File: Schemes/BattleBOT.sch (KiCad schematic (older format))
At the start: 16 parts

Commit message: make changes to Schemes
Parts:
- removed 1kΩ, 2.2kΩ: R, symbol Device:R
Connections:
- net +12V: no longer U?.~ (Vin)
- net at U?.1 (MotorB): now also M?.1 (+)
- net at U?.2: now also M?.2 (-)
- new net: U?.~ (IN3), U?.~ (Vin) (x9)
- new net: U?.~ (VCC), U?.~ (Vin)
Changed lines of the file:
@@
 Wire Wire Line
 	2650 1600 2650 1800
-Wire Wire Line
-	2650 2400 3000 2400
 $Comp
 L pspice:0 #GND?
@@
 Connection ~ 2650 1800
 Wire Wire Line
-	2650 1800 2650 2400
-Wire Wire Line
 	2650 1800 4250 1800
 Wire Wire Line
@@
 	3250 5150 3250 5100
 Wire Wire Line
-	4000 2750 6300 2750
-Wire Wire Line
-	6300 2750 6300 1750
-Wire Wire Line
-	6200 1750 6200 2600
-Wire Wire Line
-	6200 2600 4000 2600
-Wire Wire Line
 	4000 3000 6600 3000
 Wire Wire Line
 	6600 3000 6600 1750
-Wire Wire Line
-	6400 1750 6400 3200
-Wire Wire Line
-	6400 3200 4000 3200
-Wire Wire Line
-	6500 1750 6500 3300
-Wire Wire Line
-	6500 3300 4000 3300
 Wire Wire Line
 	4550 5900 6000 5900
@@
 Wire Wire Line
 	10550 1450 10550 2000
-Wire Wire Line
-	9550 2000 9100 2000
 $Comp
 L Device:R 1kΩ
@@
 	1    0    0    -1
 $EndComp
-$Comp
-L Device:R 1kΩ
-U 1 1 5E9473A1
-P 7850 2850
-F 0 "1kΩ" H 7920 2896 50  0000 L CNN
-F 1 "R" H 7920 2805 50  0000 L CNN
-F 2 "" V 7780 2850 50  0001 C CNN
-F 3 "~" H 7850 2850 50  0001 C CNN
-	1    7850 2850
-	1    0    0    -1
-$EndComp
-$Comp
-L Device:R 2.2kΩ
-U 1 1 5E9479C3
-P 7850 3150
-F 0 "2.2kΩ" H 7920 3196 50  0000 L CNN
-F 1 "R" H 7920 3105 50  0000 L CNN
-F 2 "" V 7780 3150 50  0001 C CNN
-F 3 "~" H 7850 3150 50  0001 C CNN
-	1    7850 3150
-	1    0    0    -1
-$EndComp
 Wire Wire Line
 	6100 1750 6100 3100
 Wire Wire Line
 	6100 3100 4000 3100
-Wire Wire Line
-	7850 1950 7850 1800
 Wire Wire Line
 	7850 650  4250 650
@@
 	4250 1800 5800 1800
 Wire Wire Line
-	7850 1800 7500 1800
-Wire Wire Line
-	7500 1800 7500 2700
-Wire Wire Line
-	7500 2700 7850 2700
-Connection ~ 7850 1800
-Wire Wire Line
-	7850 1800 7850 650
-Wire Wire Line
-	7850 2550 8550 2550
-Wire Wire Line
-	8550 2550 8550 3400
-Wire Wire Line
-	8550 3400 7850 3400
-Wire Wire Line
-	7850 3400 7850 3300
-$Comp
-L pspice:0 #GND?
-U 1 1 5EC7A03C
-P 7850 3600
-F 0 "#GND?" H 7850 3500 50  0001 C CNN
-F 1 "0" H 7850 3689 50  0000 C CNN
-F 2 "" H 7850 3600 50  0001 C CNN
-F 3 "~" H 7850 3600 50  0001 C CNN
-	1    7850 3600
-	1    0    0    -1
-$EndComp
-Wire Wire Line
-	7850 3400 7850 3600
-Connection ~ 7850 3400
-Wire Wire Line
-	4000 4000 7500 4000
-Wire Wire Line
-	7500 4000 7500 3000
-Wire Wire Line
-	7500 3000 7850 3000
-Connection ~ 7850 3000
-Wire Wire Line
 	4000 3900 7300 3900
 Wire Wire Line
@@
 Connection ~ 7850 2250
 Wire Wire Line
-	7850 2250 9100 2250
-Wire Wire Line
-	9100 2250 9100 2000
-Wire Wire Line
-	8950 3000 8950 1450
-Wire Wire Line
-	7850 3000 8950 3000
-Wire Wire Line
 	8950 1450 10550 1450
+Wire Wire Line
+	6000 1750 6000 2100
+Wire Wire Line
+	6000 2100 3000 2100
+Wire Wire Line
+	3000 2100 3000 2400
+Wire Wire Line
+	7850 650  7850 1950
+$Comp
+L pspice:0 #GND?
+U 1 1 5EC82388
+P 7850 2700
+F 0 "#GND?" H 7850 2600 50  0001 C CNN
+F 1 "0" H 7850 2789 50  0000 C CNN
+F 2 "" H 7850 2700 50  0001 C CNN
+F 3 "~" H 7850 2700 50  0001 C CNN
+	1    7850 2700
+	1    0    0    -1
+$EndComp
+Wire Wire Line
+	7850 2550 7850 2700
+Wire Wire Line
+	4000 4000 7500 4000
+Wire Wire Line
+	7500 4000 7500 2800
+Wire Wire Line
+	7500 2800 8950 2800
+Wire Wire Line
+	8950 2800 8950 1450
+Wire Wire Line
+	8650 2250 8650 2000
+Wire Wire Line
+	8650 2000 9550 2000
+Wire Wire Line
+	7850 2250 8650 2250
+Wire Wire Line
+	4000 3200 6200 3200
+Wire Wire Line
+	6200 3200 6200 1750
+Wire Wire Line
+	4000 3300 6300 3300
+Wire Wire Line
+	6300 3300 6300 1750
+Wire Wire Line
+	4000 3400 6500 3400
+Wire Wire Line
+	6500 3400 6500 1750
+Wire Wire Line
+	4000 3500 6400 3500
+Wire Wire Line
+	6400 3500 6400 1750
 $EndSCHEMATC

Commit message: make changes to schemes
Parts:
- added 10kΩ: R, symbol Device:R
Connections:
- net at U?.1 (MotorB): now also M?.1 (+)
- net at U?.2: now also M?.2 (-)
- net at 100nF.1, 100μF.1, U?.~ (VCC)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: now also 10kΩ.2
- new net: U?.~ (IN3), U?.~ (Vin) (x9)
- new net: U?.~ (VCC), U?.~ (Vin)
- new net: 10kΩ.1, U?.~ (VCC)
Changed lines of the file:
@@
 Connection ~ 10150 2750
 Wire Wire Line
-	10150 2750 9250 2750
+	10150 2750 9850 2750
 Wire Wire Line
 	10650 4350 10650 4550
@@
 Wire Wire Line
 	6400 3500 6400 1750
+Wire Wire Line
+	9850 2750 9850 2650
+Wire Wire Line
+	9850 2650 10550 2650
+Connection ~ 9850 2750
+Wire Wire Line
+	9850 2750 9250 2750
+$Comp
+L Device:R 10kΩ
+U 1 1 5ECBFEC7
+P 10550 2500
+F 0 "10kΩ" H 10620 2546 50  0000 L CNN
+F 1 "R" H 10620 2455 50  0000 L CNN
+F 2 "" V 10480 2500 50  0001 C CNN
+F 3 "~" H 10550 2500 50  0001 C CNN
+	1    10550 2500
+	1    0    0    -1
+$EndComp
+Wire Wire Line
+	10550 2350 10550 2300
 $EndSCHEMATC

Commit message: fix a mistake
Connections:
- net +12V: no longer 1kΩ.1
- net at 1kΩ.2, 2.2kΩ.1, U?.~ (VCC): no longer U?.~ (Vin)
- net at U?.1 (MotorB): now also M?.1 (+)
- net at U?.2: now also M?.2 (-)
- new net: U?.~ (IN3), U?.~ (Vin) (x9)
- new net: U?.~ (VCC), U?.~ (Vin)
- new net: 1kΩ.1, U?.~ (Vin)
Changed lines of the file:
@@
 Connection ~ 2650 1800
-Wire Wire Line
-	2650 1800 4250 1800
 Wire Wire Line
 	5800 1800 5800 1750
@@
 	6100 3100 4000 3100
 Wire Wire Line
-	7850 650  4250 650
-Wire Wire Line
-	4250 650  4250 1800
-Connection ~ 4250 1800
-Wire Wire Line
-	4250 1800 5800 1800
-Wire Wire Line
 	4000 3900 7300 3900
-Wire Wire Line
-	7300 3900 7300 2250
-Wire Wire Line
-	7300 2250 7850 2250
 Connection ~ 7850 2250
 Wire Wire Line
@@
 Wire Wire Line
 	3000 2100 3000 2400
-Wire Wire Line
-	7850 650  7850 1950
 $Comp
 L pspice:0 #GND?
@@
 Wire Wire Line
 	10550 2350 10550 2300
+Wire Wire Line
+	2650 1800 5800 1800
+Wire Wire Line
+	7300 1950 7850 1950
+Wire Wire Line
+	7300 1950 7300 3900
 $EndSCHEMATC

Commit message: make changes to scheme
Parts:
- added D?: D_Bridge_+-AA, symbol Device:D_Bridge_+-AA
- added SW? (x2): SW_SPST, symbol Switch:SW_SPST
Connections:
- net +12V: now also SW?.1 (A), SW?.1 (A); no longer U?.~ (IN3), U?.~ (IN3)
- net 0: now also D?.2 (-), D?.4 (~~)
- net at U?.1 (MotorB): now also M?.1 (+)
- net at U?.2: now also M?.2 (-)
- net +9V: no longer names the net of 100nF.1, 100μФ.1, U?.~ (Vcc)
- net +9V: now also D?.1 (+)
- new net: U?.~ (IN3), U?.~ (Vin) (x9)
- new net: U?.~ (VCC), U?.~ (Vin)
- new net: SW?.2 (B), U?.~ (IN3), U?.~ (IN3)
- new net: D?.3 (~~), SW?.2 (B)
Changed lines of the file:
@@
 L power:+12V #PWR?
 U 1 1 5E215B1C
-P 2650 1600
-F 0 "#PWR?" H 2650 1450 50  0001 C CNN
-F 1 "+12V" H 2665 1773 50  0000 C CNN
-F 2 "" H 2650 1600 50  0001 C CNN
-F 3 "" H 2650 1600 50  0001 C CNN
-	1    2650 1600
+P 2000 1550
+F 0 "#PWR?" H 2000 1400 50  0001 C CNN
+F 1 "+12V" H 2015 1723 50  0000 C CNN
+F 2 "" H 2000 1550 50  0001 C CNN
+F 3 "" H 2000 1550 50  0001 C CNN
+	1    2000 1550
 	1    0    0    -1
 $EndComp
@@
 Connection ~ 9850 4000
 Wire Wire Line
-	9500 4000 9550 4000
-Wire Wire Line
-	9500 3500 9500 4000
-$Comp
-L power:+9V #PWR?
-U 1 1 5E232A4E
-P 9500 3500
-F 0 "#PWR?" H 9500 3350 50  0001 C CNN
-F 1 "+9V" H 9515 3673 50  0000 C CNN
-F 2 "" H 9500 3500 50  0001 C CNN
-F 3 "" H 9500 3500 50  0001 C CNN
-	1    9500 3500
-	1    0    0    -1
-$EndComp
-Wire Wire Line
 	10150 4650 10150 4550
 $Comp
@@
 Wire Wire Line
 	7300 1950 7300 3900
+$Comp
+L Device:D_Bridge_+-AA D?
+U 1 1 5EDAFCCD
+P 8600 3800
+F 0 "D?" H 8944 3846 50  0000 L CNN
+F 1 "D_Bridge_+-AA" H 8944 3755 50  0000 L CNN
+F 2 "" H 8600 3800 50  0001 C CNN
+F 3 "~" H 8600 3800 50  0001 C CNN
+	1    8600 3800
+	1    0    0    -1
+$EndComp
+Wire Wire Line
+	8900 3800 8900 4000
+Wire Wire Line
+	8300 3800 8300 4750
+Wire Wire Line
+	8300 4750 9550 4750
+$Comp
+L pspice:0 #GND?
+U 1 1 5EDB9C3D
+P 8600 4300
+F 0 "#GND?" H 8600 4200 50  0001 C CNN
+F 1 "0" H 8600 4389 50  0000 C CNN
+F 2 "" H 8600 4300 50  0001 C CNN
+F 3 "~" H 8600 4300 50  0001 C CNN
+	1    8600 4300
+	1    0    0    -1
+$EndComp
+Wire Wire Line
+	8600 4100 8600 4300
+Wire Wire Line
+	9500 4000 9550 4000
+Wire Wire Line
+	8900 4000 9550 4000
+$Comp
+L power:+12V #PWR?
+U 1 1 5EDBC58C
+P 7950 3250
+F 0 "#PWR?" H 7950 3100 50  0001 C CNN
+F 1 "+12V" H 7965 3423 50  0000 C CNN
+F 2 "" H 7950 3250 50  0001 C CNN
+F 3 "" H 7950 3250 50  0001 C CNN
+	1    7950 3250
+	1    0    0    -1
+$EndComp
+$Comp
+L Switch:SW_SPST SW?
+U 1 1 5EDC0010
+P 2450 1600
+F 0 "SW?" H 2450 1835 50  0000 C CNN
+F 1 "SW_SPST" H 2450 1744 50  0000 C CNN
+F 2 "" H 2450 1600 50  0001 C CNN
+F 3 "~" H 2450 1600 50  0001 C CNN
+	1    2450 1600
+	1    0    0    -1
+$EndComp
+$Comp
+L Switch:SW_SPST SW?
+U 1 1 5EDC0940
+P 8250 3300
+F 0 "SW?" H 8250 3535 50  0000 C CNN
+F 1 "SW_SPST" H 8250 3444 50  0000 C CNN
+F 2 "" H 8250 3300 50  0001 C CNN
+F 3 "~" H 8250 3300 50  0001 C CNN
+	1    8250 3300
+	1    0    0    -1
+$EndComp
+Wire Wire Line
+	8450 3300 8600 3300
+Wire Wire Line
+	8600 3300 8600 3500
+Wire Wire Line
+	7950 3250 7950 3300
+Wire Wire Line
+	7950 3300 8050 3300
+Wire Wire Line
+	2000 1550 2000 1600
+Wire Wire Line
+	2000 1600 2250 1600
 $EndSCHEMATC

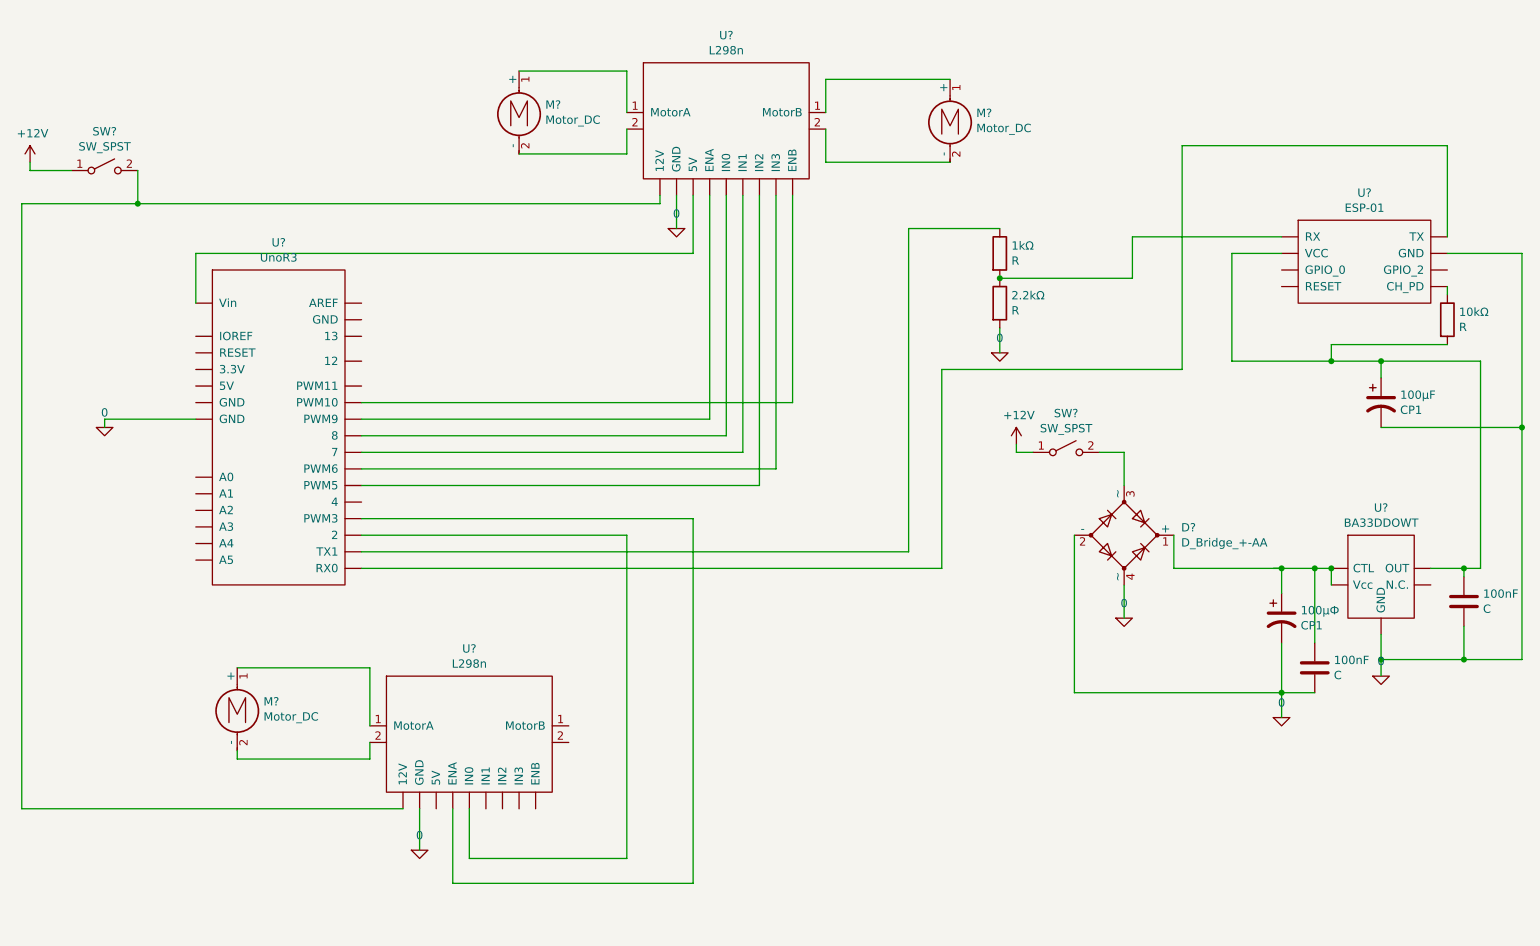
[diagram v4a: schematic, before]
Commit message: make better view of power supply
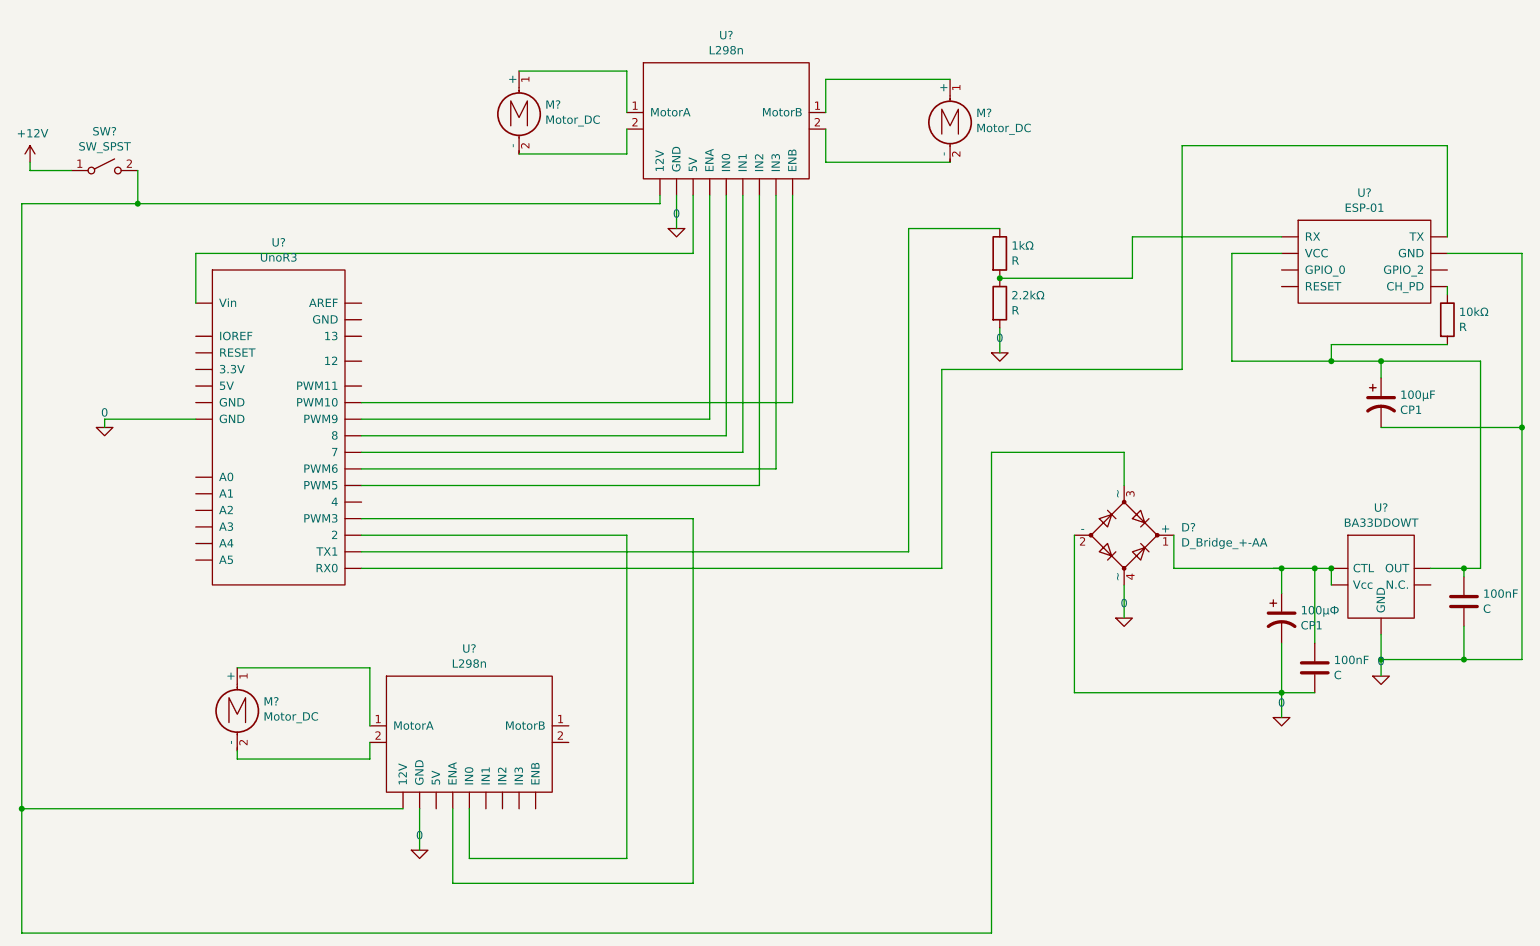
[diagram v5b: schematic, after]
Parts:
- removed SW?: SW_SPST, symbol Switch:SW_SPST
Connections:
- net at U?.1 (MotorB): now also M?.1 (+)
- net at U?.2: now also M?.2 (-)
- net at D?.3 (~~): now also SW?.2 (B), U?.~ (IN3), U?.~ (IN3)
- new net: U?.~ (IN3), U?.~ (Vin) (x9)
- new net: U?.~ (VCC), U?.~ (Vin)
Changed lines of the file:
@@
 	4250 5450 1950 5450
-Wire Wire Line
-	1950 5450 1950 1800
 Wire Wire Line
 	1950 1800 2650 1800
@@
 Wire Wire Line
 	8300 3800 8300 4750
-Wire Wire Line
-	8300 4750 9550 4750
 $Comp
 L pspice:0 #GND?
@@
 Wire Wire Line
 	8900 4000 9550 4000
-$Comp
-L power:+12V #PWR?
-U 1 1 5EDBC58C
-P 7950 3250
-F 0 "#PWR?" H 7950 3100 50  0001 C CNN
-F 1 "+12V" H 7965 3423 50  0000 C CNN
-F 2 "" H 7950 3250 50  0001 C CNN
-F 3 "" H 7950 3250 50  0001 C CNN
-	1    7950 3250
-	1    0    0    -1
-$EndComp
 $Comp
 L Switch:SW_SPST SW?
@@
 	1    0    0    -1
 $EndComp
-$Comp
-L Switch:SW_SPST SW?
-U 1 1 5EDC0940
-P 8250 3300
-F 0 "SW?" H 8250 3535 50  0000 C CNN
-F 1 "SW_SPST" H 8250 3444 50  0000 C CNN
-F 2 "" H 8250 3300 50  0001 C CNN
-F 3 "~" H 8250 3300 50  0001 C CNN
-	1    8250 3300
-	1    0    0    -1
-$EndComp
-Wire Wire Line
-	8450 3300 8600 3300
 Wire Wire Line
 	8600 3300 8600 3500
 Wire Wire Line
-	7950 3250 7950 3300
-Wire Wire Line
-	7950 3300 8050 3300
-Wire Wire Line
 	2000 1550 2000 1600
 Wire Wire Line
 	2000 1600 2250 1600
+Wire Wire Line
+	8300 4750 9550 4750
+Wire Wire Line
+	8600 3300 7800 3300
+Wire Wire Line
+	7800 3300 7800 6200
+Wire Wire Line
+	7800 6200 1950 6200
+Wire Wire Line
+	1950 1800 1950 5450
+Connection ~ 1950 5450
+Wire Wire Line
+	1950 5450 1950 6200
 $EndSCHEMATC
